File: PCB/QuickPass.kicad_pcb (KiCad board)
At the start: 2 copper layers, 20 x 67.5 mm, 12 parts, among them J1 USB_A, J2 Conn_01x04_Female, SW4 RotaryEncoder_Switch, U1 KB2040

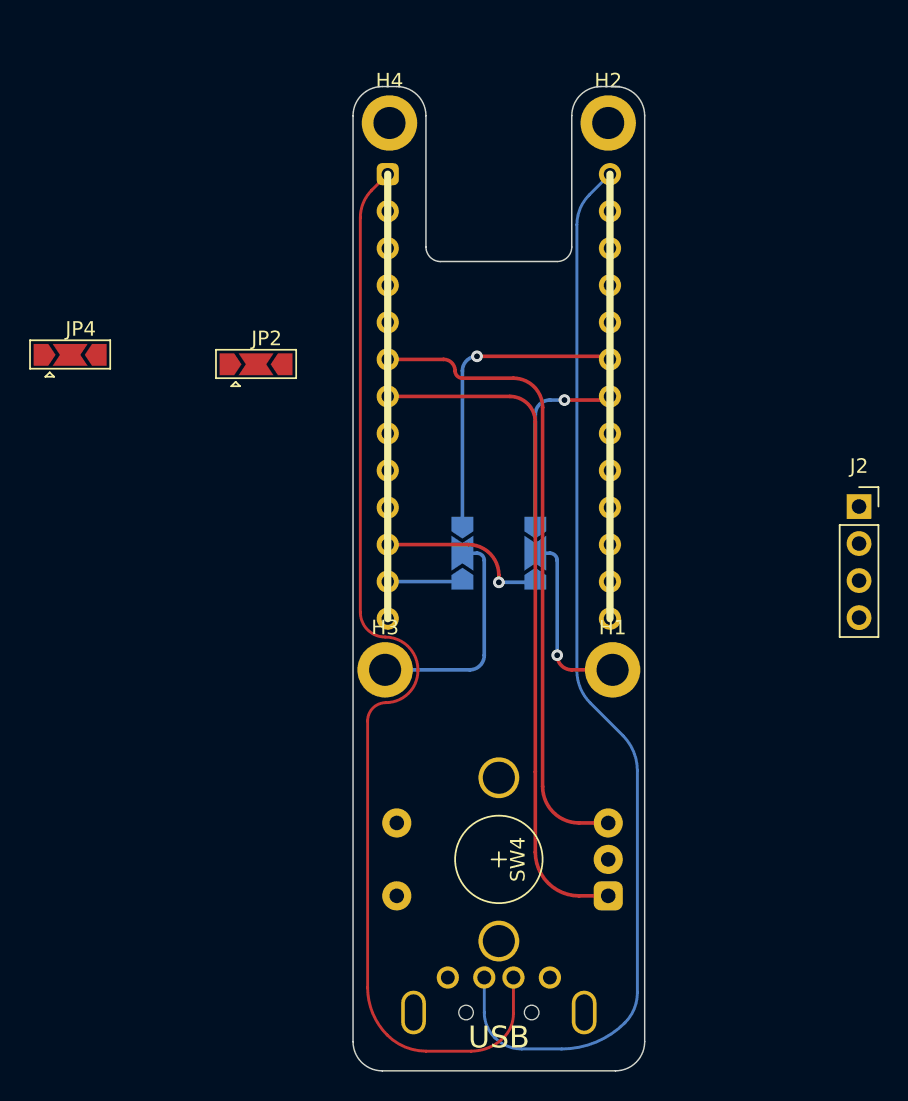
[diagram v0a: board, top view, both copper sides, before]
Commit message: add lower plate
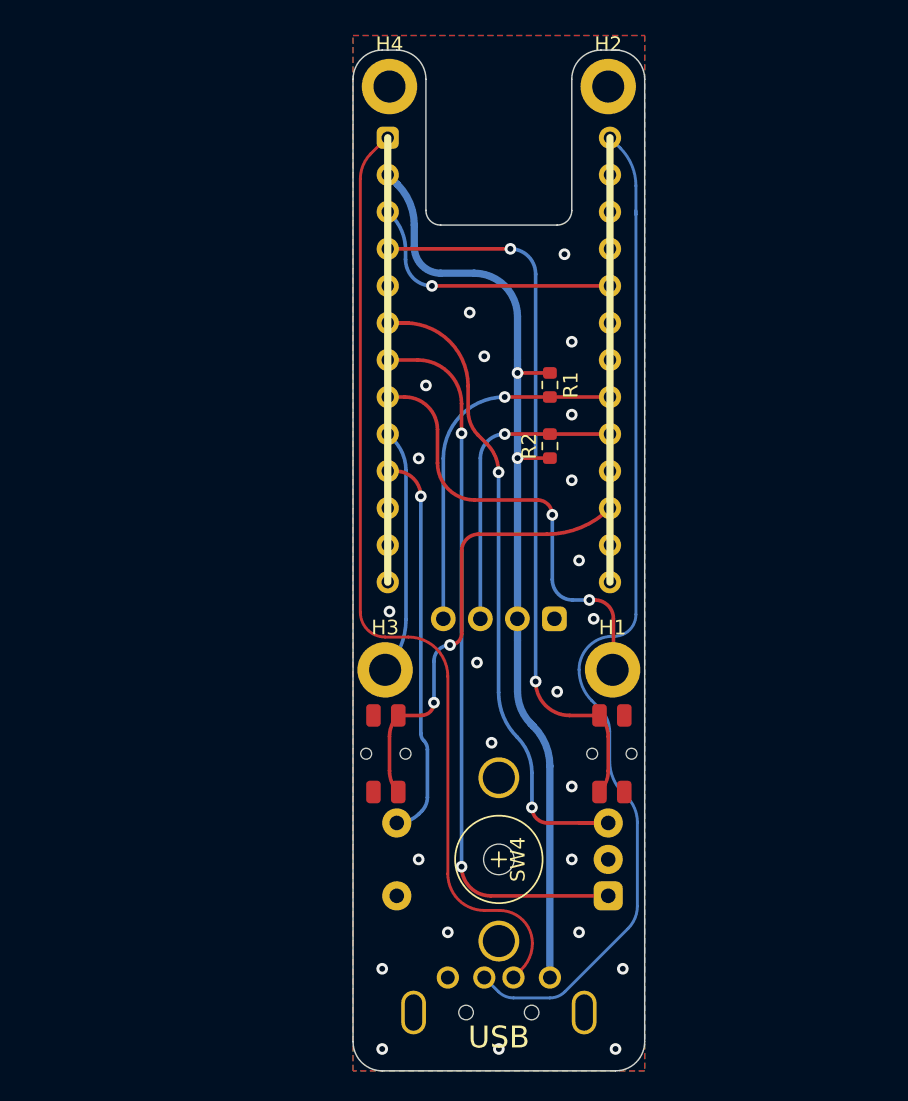
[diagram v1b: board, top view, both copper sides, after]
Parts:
- removed JP1, JP2, JP3, JP4: Jumper_3_Open, Jumper:SolderJumper-3_P2.0mm_Open_TrianglePad1.0x1.5mm
- added R1: 10k, Resistor_SMD:R_0603_1608Metric, F.Cu at (113.5, 94.0)
- added R2: 10k, Resistor_SMD:R_0603_1608Metric, F.Cu at (113.5, 98.2)
- added SW1: SW_MEC_5E, Akizuki:THAU13-AB-R, F.Cu at (117.8, 119.3)
- added SW2: SW_MEC_5E, Akizuki:THAU13-AB-R, F.Cu at (102.2, 119.3)
- moved J2 29.5 mm to (106.2, 110.0), turned to 90 degrees
- moved H2 2.50 mm to (117.5, 73.5)
- moved H4 2.50 mm to (102.5, 73.5)
- moved U1 2.50 mm to (110.0, 92.2)
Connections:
- H1 pad 1: Net-(H1-Pad1) -> /P0
- H2 pad 1: Net-(H2-Pad1) -> GND
- H3 pad 1: Net-(H3-Pad1) -> /P1
- H4 pad 1: Net-(H4-Pad1) -> GND
- U1 pad 10: /P0 -> unconnected-(U1-Pad10)
- U1 pad 11: /P1 -> unconnected-(U1-Pad11)
- U1 pad 12: /EncPB -> unconnected-(U1-Pad12)
- U1 pad 17: unconnected-(U1-Pad17) -> /SCL
- U1 pad 18: unconnected-(U1-Pad18) -> /SDA
- U1 pad 19: /SCL -> unconnected-(U1-Pad19)
- U1 pad 20: /SDA -> unconnected-(U1-Pad20)
- U1 pad 7: unconnected-(U1-Pad7) -> /P0
- U1 pad 8: unconnected-(U1-Pad8) -> /P1
- U1 pad 9: unconnected-(U1-Pad9) -> /EncPB
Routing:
- net VBUS: track 0.00 -> 65.5 mm, vias 0 -> 2
- net /RST: track 0.00 -> 51.0 mm, vias 0 -> 2
- net /S0: track 0.00 -> 31.6 mm, vias 0 -> 2
- net /EncPB: track 0.00 -> 26.9 mm, vias 0 -> 1
- net GND: track 0.00 -> 18.6 mm, vias 0 -> 25
- net /P0: track 11.7 -> 30.2 mm, vias 1 -> 2
- net Net-(H3-Pad1): track 15.6 -> 0.00 mm
- net Net-(H1-Pad1): track 12.6 -> 0.00 mm, vias 1 -> 0
- net /P1: track 5.17 -> 16.9 mm
- net /D-: track 76.7 -> 66.2 mm
- net /SCL: track 13.3 -> 20.8 mm
- net /D+: track 74.5 -> 70.8 mm
- net /SDA: track 21.3 -> 24.7 mm
- net /EncB: track 47.1 -> 49.5 mm, vias 0 -> 2
- net /EncA: track 44.2 -> 46.0 mm, vias 0 -> 2
- added copper zone on B.Cu, net GND
- added copper zone on F.Cu, net GND
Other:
- board size 20 x 67.5 mm -> 20 x 70 mm
